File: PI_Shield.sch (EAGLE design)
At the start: 29 parts, among them Q1 8MHz, Q2 220mA/50V/3.5Ω

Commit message: Made Changes to Schematic
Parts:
- removed Q1: 8MHz, crystal:CRYSTALHC33U-V
- added Y1: ECS-80-S-4X, ECS-80-S-4X:ECS-80-S-4X
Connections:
- net 3V3: now also R5.2; no longer D2.A
- net N$4: now also D2.C; no longer R5.1
- net N$5: now also D2.A, R5.1; no longer D2.C, R5.2
- net OSC1: now also Y1.1; no longer Q1.1
- net OSC2: now also Y1.2; no longer Q1.2
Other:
- moved on the sheet: C1, D2, R5
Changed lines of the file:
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@@
 <part name="R2" library="SparkFun-Resistors" library_urn="urn:adsk.eagle:library:532" deviceset="RESISTOR" device="0603" package3d_urn="urn:adsk.eagle:package:39650/1" value="1k"/>
 <part name="D1" library="SparkFun-DiscreteSemi" library_urn="urn:adsk.eagle:library:514" deviceset="DIODE" device="-1N4148" package3d_urn="urn:adsk.eagle:package:38452/1" value="200mA/100V/1V"/>
-<part name="Q1" library="crystal" library_urn="urn:adsk.eagle:library:204" deviceset="CRYSTAL" device="HC33U-V" package3d_urn="urn:adsk.eagle:package:12084/1" value="8MHz"/>
 <part name="C4" library="SparkFun-Capacitors" library_urn="urn:adsk.eagle:library:510" deviceset="22NF/22,000PF" device="-0603-50V-10%" package3d_urn="urn:adsk.eagle:package:37414@1/1" value="22nF"/>
 <part name="C1" library="SparkFun-Capacitors" library_urn="urn:adsk.eagle:library:510" deviceset="22PF" device="-0603-50V-5%" package3d_urn="urn:adsk.eagle:package:37414@1/1" value="22pF"/>
@@
 <part name="J2" library="SparkFun-Connectors" library_urn="urn:adsk.eagle:library:513" deviceset="CONN_02" device="" package3d_urn="urn:adsk.eagle:package:38039/1"/>
 <part name="J5" library="SparkFun-Connectors" library_urn="urn:adsk.eagle:library:513" deviceset="CONN_04" device="" package3d_urn="urn:adsk.eagle:package:38085/1"/>
+<part name="Y1" library="ECS-80-S-4X" deviceset="ECS-80-S-4X" device=""/>
 </parts>
 <sheets>
@@
 <instance part="R2" gate="G$1" x="119.38" y="68.58" rot="R90"/>
 <instance part="D1" gate="G$1" x="129.54" y="66.04" rot="R90"/>
-<instance part="Q1" gate="G$1" x="50.8" y="66.04" rot="R90"/>
 <instance part="C4" gate="G$1" x="119.38" y="53.34"/>
-<instance part="C1" gate="G$1" x="38.1" y="71.12" rot="R90"/>
+<instance part="C1" gate="G$1" x="38.1" y="76.2" rot="R90"/>
 <instance part="C2" gate="G$1" x="38.1" y="60.96" rot="R90"/>
 <instance part="U$2" gate="G$1" x="147.32" y="134.62"/>
@@
 <instance part="R4" gate="G$1" x="190.5" y="60.96" rot="R90"/>
 <instance part="Q2" gate="NMOS" x="203.2" y="48.26"/>
-<instance part="R5" gate="G$1" x="220.98" y="60.96" rot="R90"/>
-<instance part="D2" gate="G$1" x="220.98" y="73.66"/>
+<instance part="R5" gate="G$1" x="220.98" y="73.66" rot="R90"/>
+<instance part="D2" gate="G$1" x="220.98" y="63.5"/>
 <instance part="C3" gate="G$1" x="91.44" y="142.24" rot="R270"/>
 <instance part="C5" gate="G$1" x="119.38" y="142.24" rot="R90"/>
@@
 <instance part="C6" gate="G$1" x="200.66" y="127"/>
 <instance part="J2" gate="G$1" x="228.6" y="132.08"/>
+<instance part="Y1" gate="G$1" x="48.26" y="68.58" rot="R90"/>
 </instances>
 <busses>
@@
 </segment>
 <segment>
-<wire x1="33.02" y1="71.12" x2="25.4" y2="71.12" width="0.1524" layer="91"/>
 <wire x1="25.4" y1="71.12" x2="25.4" y2="60.96" width="0.1524" layer="91"/>
 <wire x1="25.4" y1="60.96" x2="25.4" y2="53.34" width="0.1524" layer="91"/>
 <wire x1="33.02" y1="60.96" x2="25.4" y2="60.96" width="0.1524" layer="91"/>
 <junction x="25.4" y="60.96"/>
-<pinref part="C1" gate="G$1" pin="1"/>
 <pinref part="C2" gate="G$1" pin="1"/>
 <label x="22.86" y="50.8" size="1.778" layer="95"/>
+<pinref part="C1" gate="G$1" pin="1"/>
+<wire x1="33.02" y1="76.2" x2="25.4" y2="76.2" width="0.1524" layer="91"/>
+<wire x1="25.4" y1="76.2" x2="25.4" y2="71.12" width="0.1524" layer="91"/>
 </segment>
 </net>
@@
 </segment>
 <segment>
-<wire x1="40.64" y1="60.96" x2="50.8" y2="60.96" width="0.1524" layer="91"/>
-<pinref part="Q1" gate="G$1" pin="1"/>
-<wire x1="50.8" y1="60.96" x2="50.8" y2="63.5" width="0.1524" layer="91"/>
+<wire x1="40.64" y1="60.96" x2="48.26" y2="60.96" width="0.1524" layer="91"/>
+<wire x1="48.26" y1="60.96" x2="50.8" y2="60.96" width="0.1524" layer="91"/>
 <wire x1="50.8" y1="60.96" x2="60.96" y2="60.96" width="0.1524" layer="91"/>
-<junction x="50.8" y="60.96"/>
 <label x="55.88" y="60.96" size="1.778" layer="95"/>
 <pinref part="C2" gate="G$1" pin="2"/>
+<pinref part="Y1" gate="G$1" pin="1"/>
+<wire x1="48.26" y1="63.5" x2="48.26" y2="60.96" width="0.1524" layer="91"/>
+<junction x="48.26" y="60.96"/>
 </segment>
 </net>
@@
 </segment>
 <segment>
-<wire x1="40.64" y1="71.12" x2="50.8" y2="71.12" width="0.1524" layer="91"/>
-<pinref part="Q1" gate="G$1" pin="2"/>
-<wire x1="50.8" y1="71.12" x2="50.8" y2="68.58" width="0.1524" layer="91"/>
-<wire x1="50.8" y1="71.12" x2="60.96" y2="71.12" width="0.1524" layer="91"/>
-<junction x="50.8" y="71.12"/>
-<label x="55.88" y="71.12" size="1.778" layer="95"/>
+<wire x1="50.8" y1="76.2" x2="60.96" y2="76.2" width="0.1524" layer="91"/>
+<label x="55.88" y="76.2" size="1.778" layer="95"/>
+<pinref part="Y1" gate="G$1" pin="2"/>
+<wire x1="48.26" y1="73.66" x2="48.26" y2="76.2" width="0.1524" layer="91"/>
+<wire x1="48.26" y1="76.2" x2="50.8" y2="76.2" width="0.1524" layer="91"/>
 <pinref part="C1" gate="G$1" pin="2"/>
+<wire x1="40.64" y1="76.2" x2="48.26" y2="76.2" width="0.1524" layer="91"/>
+<junction x="48.26" y="76.2"/>
 </segment>
 </net>
@@
 <pinref part="R3" gate="G$1" pin="1"/>
 <wire x1="172.72" y1="142.24" x2="172.72" y2="144.78" width="0.1524" layer="91"/>
-</segment>
-</net>
-<net name="N$4" class="0">
-<segment>
-<pinref part="Q2" gate="NMOS" pin="D"/>
-<wire x1="205.74" y1="53.34" x2="205.74" y2="55.88" width="0.1524" layer="91"/>
-<pinref part="R5" gate="G$1" pin="1"/>
-<wire x1="205.74" y1="55.88" x2="220.98" y2="55.88" width="0.1524" layer="91"/>
-</segment>
-</net>
-<net name="N$5" class="0">
-<segment>
-<pinref part="R5" gate="G$1" pin="2"/>
-<pinref part="D2" gate="G$1" pin="C"/>
-<wire x1="220.98" y1="66.04" x2="220.98" y2="68.58" width="0.1524" layer="91"/>
 </segment>
 </net>
@@
 <wire x1="172.72" y1="154.94" x2="172.72" y2="157.48" width="0.1524" layer="91"/>
 <label x="170.18" y="157.48" size="1.778" layer="95"/>
-</segment>
-<segment>
-<pinref part="R4" gate="G$1" pin="2"/>
-<wire x1="190.5" y1="78.74" x2="190.5" y2="66.04" width="0.1524" layer="91"/>
-<label x="187.96" y="78.74" size="1.778" layer="95"/>
-</segment>
-<segment>
-<pinref part="D2" gate="G$1" pin="A"/>
-<wire x1="220.98" y1="76.2" x2="220.98" y2="78.74" width="0.1524" layer="91"/>
-<label x="218.44" y="78.74" size="1.778" layer="95"/>
 </segment>
 <segment>
@@
 <label x="121.92" y="78.74" size="1.778" layer="95"/>
 </segment>
-</net>
+<segment>
+<pinref part="R5" gate="G$1" pin="2"/>
+<wire x1="220.98" y1="78.74" x2="220.98" y2="81.28" width="0.1524" layer="91"/>
+<label x="218.44" y="81.28" size="1.778" layer="95"/>
+</segment>
+<segment>
+<pinref part="R4" gate="G$1" pin="2"/>
+<wire x1="190.5" y1="66.04" x2="190.5" y2="81.28" width="0.1524" layer="91"/>
+<label x="187.96" y="81.28" size="1.778" layer="95"/>
+</segment>
+</net>
+<net name="N$4" class="0">
+<segment>
+<pinref part="Q2" gate="NMOS" pin="D"/>
+<wire x1="205.74" y1="53.34" x2="205.74" y2="55.88" width="0.1524" layer="91"/>
+<wire x1="205.74" y1="55.88" x2="220.98" y2="55.88" width="0.1524" layer="91"/>
+<pinref part="D2" gate="G$1" pin="C"/>
+<wire x1="220.98" y1="55.88" x2="220.98" y2="58.42" width="0.1524" layer="91"/>
+</segment>
+</net>
+<net name="N$5" class="0">
+<segment>
+<pinref part="D2" gate="G$1" pin="A"/>
+<pinref part="R5" gate="G$1" pin="1"/>
+<wire x1="220.98" y1="66.04" x2="220.98" y2="68.58" width="0.1524" layer="91"/>
+</segment>
+</net>

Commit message: Starting to Route Board
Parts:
- removed J5: (no value), SparkFun-Connectors:CONN_04
- added C8, C9: .1uF, SparkFun-Capacitors:22NF/22,000PF-0603-50V-10%
- added J6: (no value), SparkFun-Connectors:CONN_03
- added J7: (no value), SparkFun-Connectors:CONN_04
- added Q1, Q3: 220mA/50V/3.5Ω, SparkFun-DiscreteSemi:MOSFET-NCH-BSS138
- added R10: 47, SparkFun-Resistors:RESISTOR0603
- added R11: 0, SparkFun-Resistors:RESISTOR0603
- added R12, R13, R14, R15: 10k, SparkFun-Resistors:RESISTOR0603
- added U1: MAX1136EUA-T, MAX1136EUA-T:MAX1136EUA-T
- C1, C2: value 22pF -> 18pF
- R3: value (none) -> 0
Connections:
- new net AIN: J6.1, U1.AIN0
- new net N$6: D1.A, R10.2
- new net N$7: C8.2
- new net SCL_ADC: Q1.D, R14.2, U1.SCL
- new net SDA_ADC: Q3.D, R13.2, U1.SDA
- net 3V3: now also Q1.G, Q3.G, R12.2, R15.2
- net 5V: now also C8.1, C9.1, J6.2, J7.4, R13.1, R14.1, U1.AIN3/REF, U1.VDD; no longer J5.4
- net GND: now also C9.2, J6.3, J7.1, U1.GND; no longer J5.1
- net IMU_RESET: now also PCB1.GPIO13; no longer PCB1.GPIO4
- net INT: now also PCB1.GPIO19, U$3.INT; no longer PCB1.GPIO7
- net N$3: now also R10.1; no longer D1.A
- net OSC2: now also R11.1, R11.2
- net RESET: now also PCB1.GPIO22; no longer PCB1.GPIO25
- net SCL: now also J7.2, Q1.S, R15.1; no longer J5.2
- net SDA: now also J7.3, Q3.S, R12.1; no longer J5.3

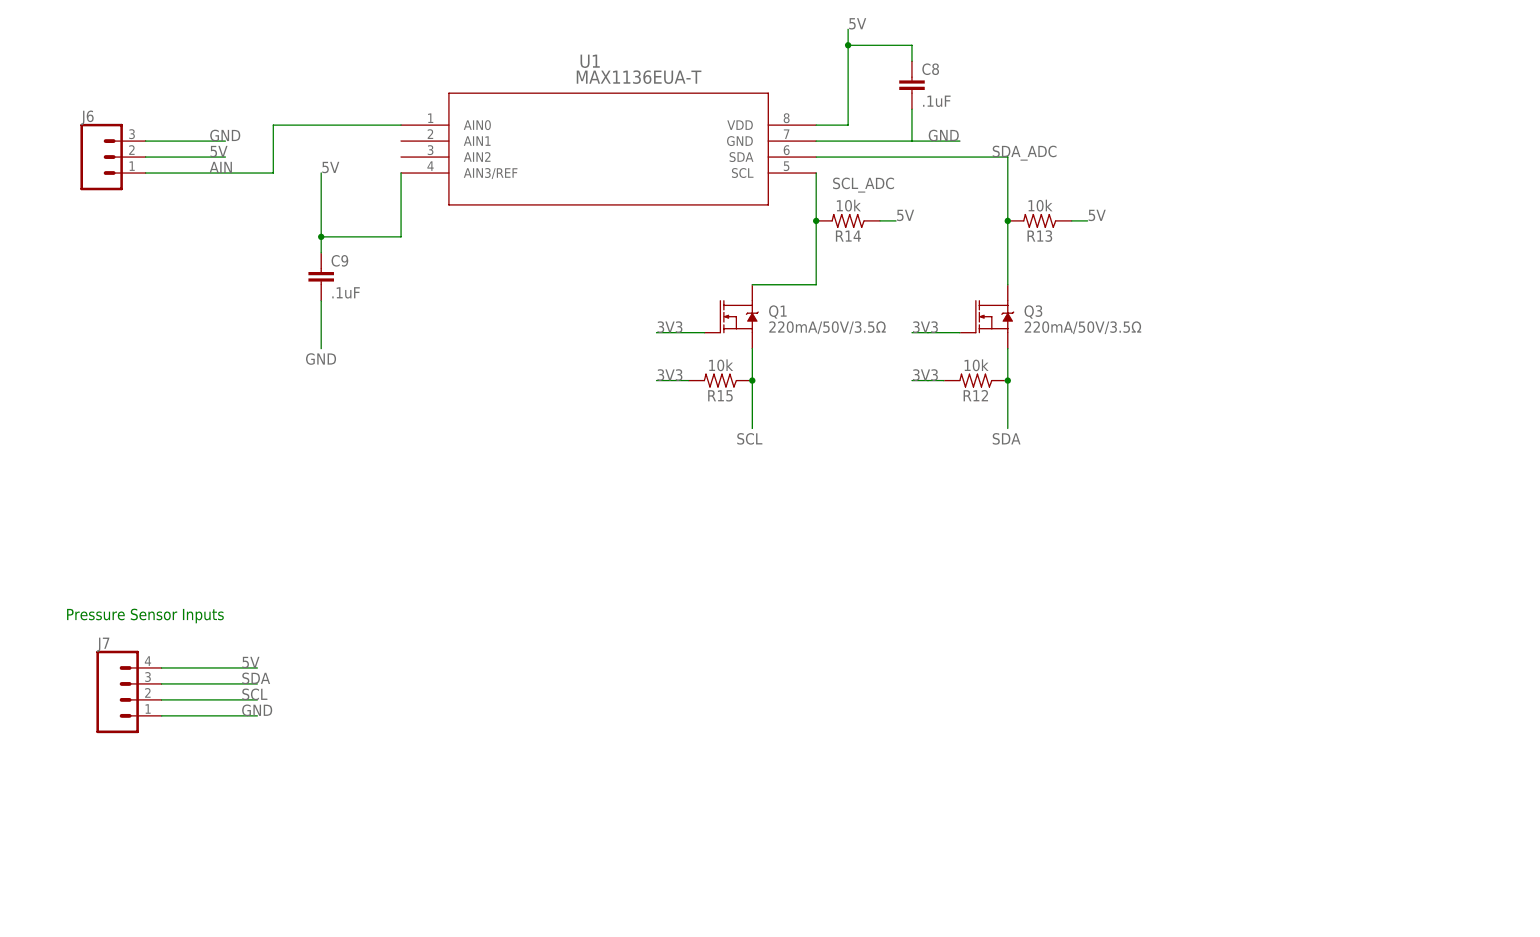
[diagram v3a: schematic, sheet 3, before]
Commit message: Added Current Sensor
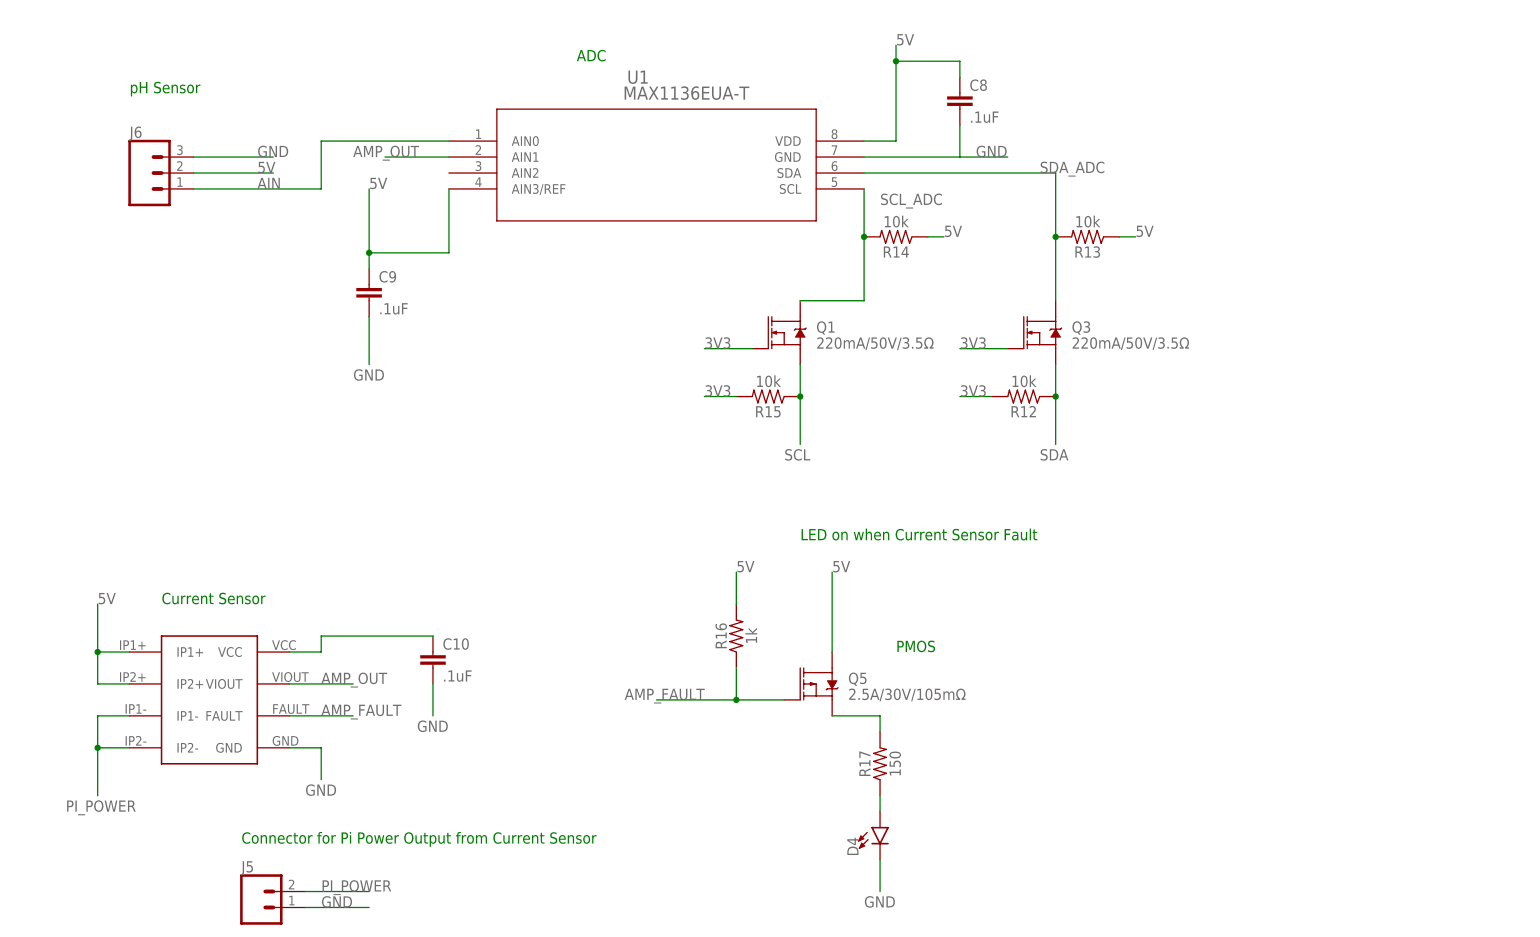
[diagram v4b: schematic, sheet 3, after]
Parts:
- removed J1: (no value), SparkFun-Connectors:CONN_03
- removed J7: (no value), SparkFun-Connectors:CONN_04
- added C10: .1uF, SparkFun-Capacitors:22NF/22,000PF-0603-50V-10%
- added D4: (no value), SparkFun-LED:LED0603
- added H1, H2, H3: MOUNT-PAD-ROUND3.6, holes:MOUNT-PAD-ROUND3.6
- added J5: (no value), SparkFun-Connectors:CONN_02
- added Q5: 2.5A/30V/105mΩ, SparkFun-DiscreteSemi:MOSFET_PCH-DMG2307L
- added R16: 1k, SparkFun-Resistors:RESISTOR0603
- added R17: 150, SparkFun-Resistors:RESISTOR0603
- added U$4, U$6, U$7: DF13-4P-1.25DSA, con-hirose-df13:DF13-4P-1.25DSA
- added U$5: ACS711, ACS711_ameter:ACS711
- renumbered Q2 to Q4
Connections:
- new net AMP_FAULT: Q5.G, R16.1, U$5.FAULT
- new net AMP_OUT: U$5.VIOUT, U1.AIN1
- new net N$10: Q5.S, R17.2
- new net N$11: D4.A, R17.1
- new net N$8: C10.1, U$5.VCC
- new net PI_POWER: J5.2, U$5.IP1-, U$5.IP2-
- net 3V3: now also H2.MOUNT, U$4.1, U$6.1, U$7.1; no longer J1.2
- net 5V: now also H1.MOUNT, Q5.D, R16.2, U$5.IP1+, U$5.IP2+; no longer J1.3, J7.4
- net GND: now also C10.2, D4.C, H3.MOUNT, J5.1, U$4.4, U$5.GND, U$6.4, U$7.4; no longer J1.1, J7.1
- net SCL: now also U$4.3, U$6.3, U$7.3; no longer J7.2
- net SDA: now also U$4.2, U$6.2, U$7.2; no longer J7.3
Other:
- note added: "ADC"
- note added: "BNO055 IMU"
- note added: "Connector for Pi Power Output from Current Sensor"
- note added: "Connectors to measure signals"
- note added: "Current Sensor"
- note added: "LED on when Current Sensor Fault"
- note added: "NMOS"
- note added: "PMOS"
- note added: "Potential pH Sensor Connector"
- note added: "Power Supply Connectors"
- note added: "Pressure Sensor Connector"
- note added: "Temperature Sensor Connector"
- note added: "pH Sensor"
- note removed: "Pressure Sensor Inputs"
- moved on the sheet: C7, C8, C9, J3, J4, J6, Q1, Q3, R12, R13, R14, R15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

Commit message: Almost Done with Board
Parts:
- removed C7: 0.1u, SparkFun-Passives:CAP0603-CAP
- removed H2: MOUNT-PAD-ROUND3.6, holes:MOUNT-PAD-ROUND3.6
- removed J2: (no value), SparkFun-Connectors:CONN_02
- removed J6: (no value), SparkFun-Connectors:CONN_03
- added C11, C12: .1uF, SparkFun-Capacitors:22NF/22,000PF-0603-50V-10%
- added C13: .1u, SparkFun-Capacitors:22NF/22,000PF-0603-50V-10%
- added D3: (no value), SparkFun-LED:LED0603
- added R18: 150, SparkFun-Resistors:RESISTOR0603
- added R19: 0, SparkFun-Resistors:RESISTOR0603
- added U$10: T2I, BackplaneParts:T2I
- added U$11, U$9: DF13-3P-1.25DSA, con-hirose-df13:DF13-3P-1.25DSA
- added U$8: T2I5P, BackplaneParts:T2I5P
- added U2: AZ1117EH-3.3TRG1, AZ1117EH-3.3TRG1:AZ1117EH-3.3TRG1
- D1: value 200mA/100V/1V -> 250mA/100V; device SparkFun-DiscreteSemi:DIODE-1N4148 -> SparkFun-DiscreteSemi:DIODE-BAS16J
- R8, R9: device resistor:R-US_R0603 -> SparkFun-Resistors:RESISTOR0603
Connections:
- removed net N$7: C8.2
- removed net N$8: C10.1, U$5.VCC
- new net DI: PCB1.GPIO23, U$9.2
- new net IMU_INT: U$3.INT
- new net IMU_NET: PCB1.GPIO6
- new net N$9: D3.A, R18.1
- net 3V3: now also C10.1, C12.1, C13.1, R8.1, R9.1, U$5.VCC, U2.OUT; no longer C7.1, H2.MOUNT, R8.2, R9.2
- net 5V: now also C11.1, R18.2, U$11.2, U$8.4, U$8.5, U$9.1, U2.IN; no longer J6.2
- net AIN: now also U$11.1; no longer J6.1
- net CANH: now also J5.2, U$10.2; no longer J2.2
- net CANL: now also J5.1, U$10.3; no longer J2.1
- net GND: now also C11.2, C12.2, C13.2, C8.2, D3.C, PCB1.GND@9, U$11.3, U$8.1, U$8.2, U$9.3, U2.ADJ/GND; no longer C7.2, J5.1, J6.3
- net INT: no longer U$3.INT
- net OSC1: now also R19.1, R19.2
- net PI_POWER: now also PCB1.5V@2, PCB1.5V@4; no longer J5.2
- net RESET: no longer PCB1.GPIO22
- net SCL: now also R9.2; no longer R9.1
- net SDA: now also R8.2; no longer R8.1
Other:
- note added: "Analog pH Sensor"
- note added: "External Power Supply Connectors"
- note added: "LED to Indicate Power is ON"
- note added: "Potential Temperature Sensor Connector"
- note removed: "Connector for Pi Power Output from Current Sensor"
- note removed: "pH Sensor"
- moved on the sheet: C8, H3, J3, J4, R8, R9, U$4, U$6, U$7
